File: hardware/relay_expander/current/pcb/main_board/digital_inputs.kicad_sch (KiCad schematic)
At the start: 22 parts, among them J12 Screw_Terminal_01x02, J13 Screw_Terminal_01x02, J14 Screw_Terminal_01x02, J15 Screw_Terminal_01x02, U4 TCMT4100, U5 TCMT4100

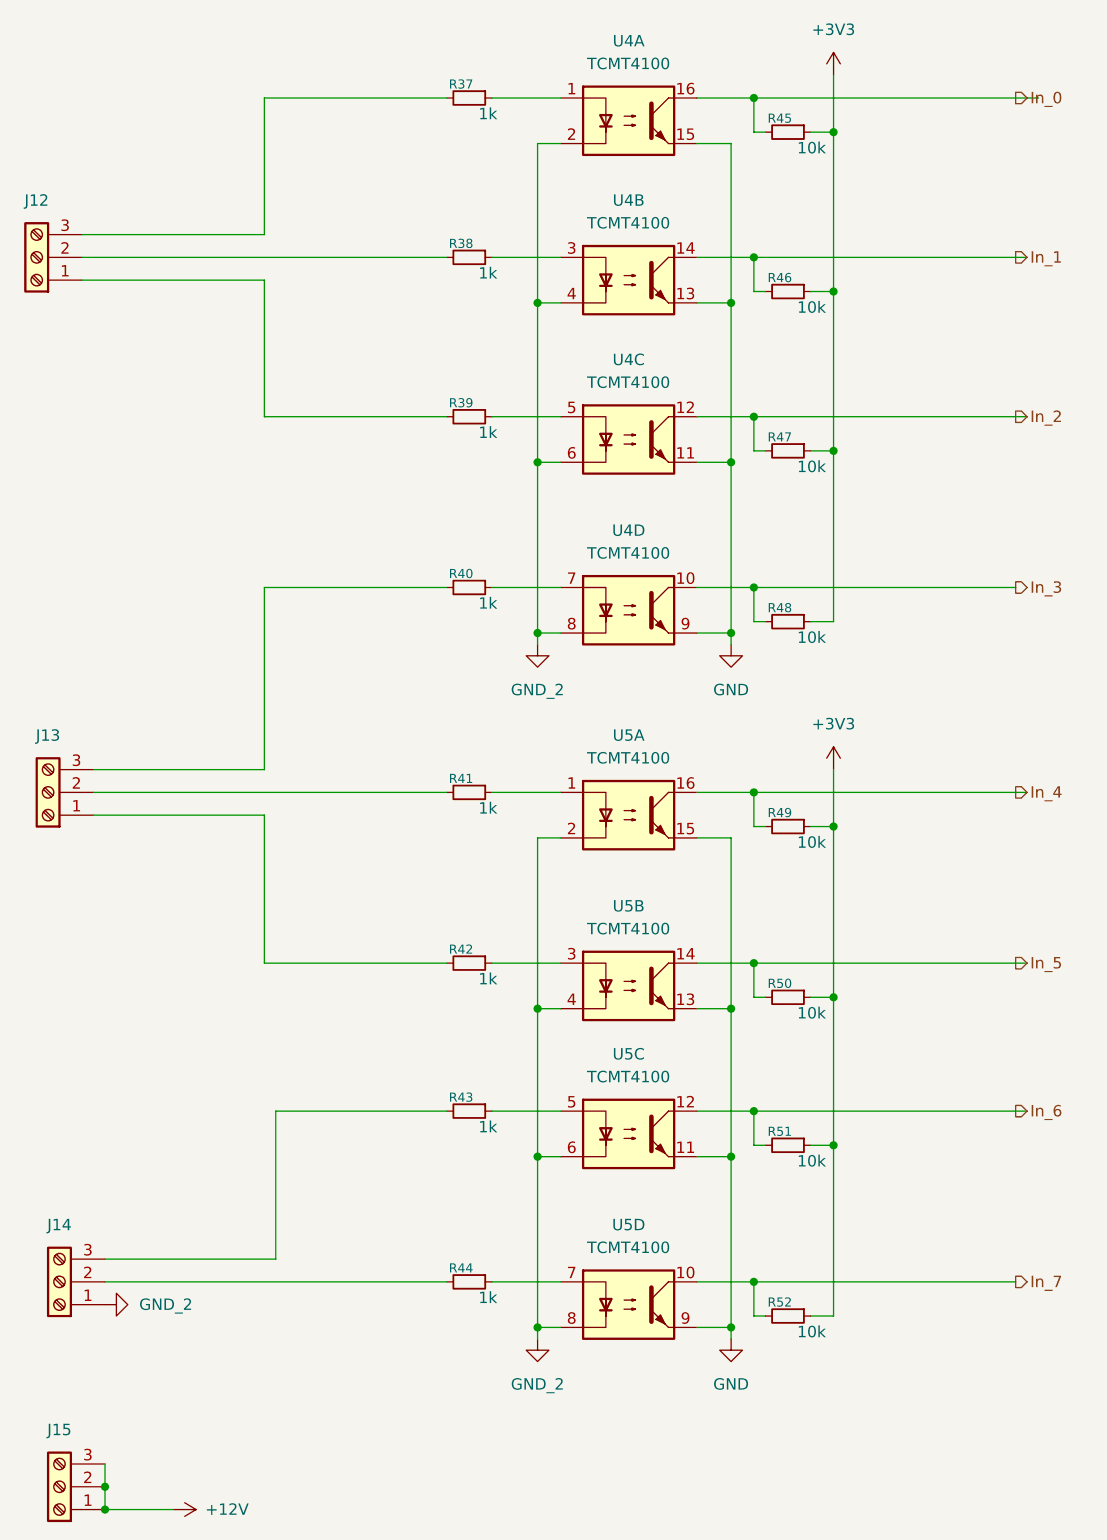
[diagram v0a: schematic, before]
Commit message: [ADD] ui board template
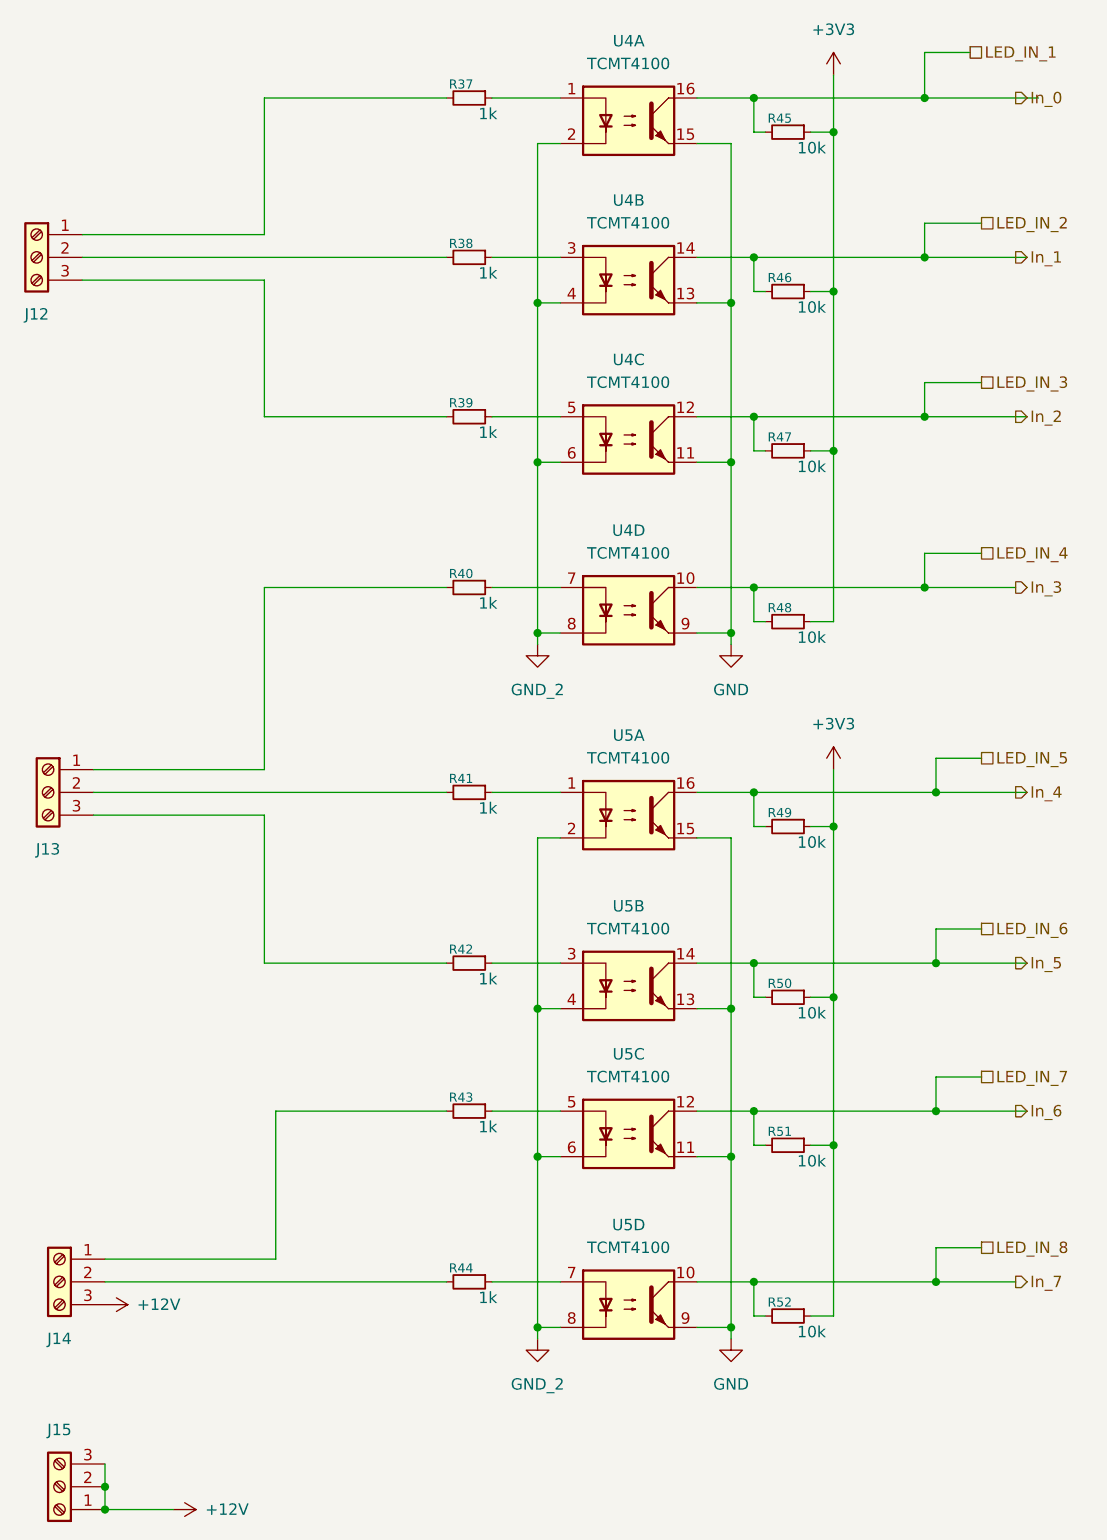
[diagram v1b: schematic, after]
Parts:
- J12, J13, J14, J15: footprint Project_Parts_Footprints_Lib:TerminalBlock_Phoenix_MPT-0,5-3-2.54_1x03_P2.54mm_Horizontal -> footprints:Terminal_block_1x3_2,54
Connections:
- net +12V: now also J14.3 (Pin_3)
- net GND_2: no longer J14.1 (Pin_1)
- net at R39.2: now also J12.3 (Pin_3); no longer J12.1 (Pin_1)
- net at R37.2: now also J12.1 (Pin_1); no longer J12.3 (Pin_3)
- net at R42.2: now also J13.3 (Pin_3); no longer J13.1 (Pin_1)
- net at R40.2: now also J13.1 (Pin_1); no longer J13.3 (Pin_3)
- net at R43.2: now also J14.1 (Pin_1); no longer J14.3 (Pin_3)
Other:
- moved on the sheet: J12, J13, J14

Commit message: [ADD] routing on main pcb board
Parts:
- J12, J13, J14, J15: footprint footprints:Terminal_block_1x3_2,54 -> TerminalBlock_Phoenix:TerminalBlock_Phoenix_MPT-0,5-3-2.54_1x03_P2.54mm_Horizontal
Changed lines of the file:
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@@
 			)
 		)
-		(property "Footprint" "footprints:Terminal_block_1x3_2,54"
+		(property "Footprint" "TerminalBlock_Phoenix:TerminalBlock_Phoenix_MPT-0,5-3-2.54_1x03_P2.54mm_Horizontal"
 			(at 90.17 180.34 0)
 			(hide yes)
@@
 			)
 		)
-		(property "Footprint" "footprints:Terminal_block_1x3_2,54"
+		(property "Footprint" "TerminalBlock_Phoenix:TerminalBlock_Phoenix_MPT-0,5-3-2.54_1x03_P2.54mm_Horizontal"
 			(at 87.63 43.18 0)
 			(hide yes)
@@
 			)
 		)
-		(property "Footprint" "footprints:Terminal_block_1x3_2,54"
+		(property "Footprint" "TerminalBlock_Phoenix:TerminalBlock_Phoenix_MPT-0,5-3-2.54_1x03_P2.54mm_Horizontal"
 			(at 88.9 102.87 0)
 			(hide yes)
@@
 			)
 		)
-		(property "Footprint" "footprints:Terminal_block_1x3_2,54"
+		(property "Footprint" "TerminalBlock_Phoenix:TerminalBlock_Phoenix_MPT-0,5-3-2.54_1x03_P2.54mm_Horizontal"
 			(at 90.17 157.48 0)
 			(hide yes)

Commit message: [FIX] add 12V trace for expanders and generate gerber for all relays related boards
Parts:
- J12, J13, J14, J15: value Screw_Terminal_01x02 -> Screw_Terminal_01x03
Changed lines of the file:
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@@
 			)
 		)
-		(property "Value" "Screw_Terminal_01x02"
+		(property "Value" "Screw_Terminal_01x03"
 			(at 87.63 177.8001 0)
 			(hide yes)
@@
 			)
 		)
-		(property "Value" "Screw_Terminal_01x02"
+		(property "Value" "Screw_Terminal_01x03"
 			(at 85.09 45.7199 0)
 			(hide yes)
@@
 			)
 		)
-		(property "Value" "Screw_Terminal_01x02"
+		(property "Value" "Screw_Terminal_01x03"
 			(at 86.36 105.4099 0)
 			(hide yes)
@@
 			)
 		)
-		(property "Value" "Screw_Terminal_01x02"
+		(property "Value" "Screw_Terminal_01x03"
 			(at 87.63 160.0199 0)
 			(hide yes)
